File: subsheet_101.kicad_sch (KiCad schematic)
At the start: 0 parts

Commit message: place les principaux circuits -- il manque le symbole pour le PIA MC6821
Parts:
- added U?: GATE_ARRAY_MO5_V1_PHY, Package_LCC:PLCC-68_THT-Socket, symbol gate_array_v1:GATE_ARRAY_MO5_V1_PHY
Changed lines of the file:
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@@
 (kicad_sch (version 20211123) (generator eeschema)
-  (paper "A4")
+  (paper "A4" portrait)
   (title_block
     (date "2023-05-12")
     (rev "DRAFT")
   )
+  (symbol (lib_id "gate_array_v1:GATE_ARRAY_MO5_V1_PHY") (at 100.33 109.22 0) (unit 1)
+    (in_bom yes) (on_board yes)
+    (property "Reference" "U?" (id 0) (at 119.38 68.58 0)
+      (effects (font (size 1.27 1.27)) (justify left top))
+    )
+    (property "Value" "GATE_ARRAY_MO5_V1_PHY" (id 1) (at 119.38 71.12 0)
+      (effects (font (size 1.27 1.27) bold) (justify left top))
+    )
+    (property "Footprint" "Package_LCC:PLCC-68_THT-Socket" (id 2) (at 119.38 66.04 0)
+      (effects (font (size 1.27 1.27)) (justify left top) hide)
+    )
+    (property "Datasheet" "" (id 3) (at 100.33 109.22 0)
+      (effects (font (size 1.27 1.27)) hide)
+    )
+    (pin "1")
+    (pin "10")
+    (pin "11")
+    (pin "12")
+    (pin "13")
+    (pin "14")
+    (pin "15")
+    (pin "16")
+    (pin "17")
+    (pin "18")
+    (pin "19")
+    (pin "2")
+    (pin "20")
+    (pin "21")
+    (pin "22")
+    (pin "23")
+    (pin "24")
+    (pin "25")
+    (pin "26")
+    (pin "27")
+    (pin "28")
+    (pin "29")
+    (pin "3")
+    (pin "30")
+    (pin "31")
+    (pin "32")
+    (pin "33")
+    (pin "34")
+    (pin "35")
+    (pin "36")
+    (pin "37")
+    (pin "38")
+    (pin "39")
+    (pin "4")
+    (pin "40")
+    (pin "41")
+    (pin "42")
+    (pin "43")
+    (pin "44")
+    (pin "45")
+    (pin "46")
+    (pin "47")
+    (pin "48")
+    (pin "49")
+    (pin "5")
+    (pin "50")
+    (pin "51")
+    (pin "52")
+    (pin "53")
+    (pin "54")
+    (pin "55")
+    (pin "56")
+    (pin "57")
+    (pin "58")
+    (pin "59")
+    (pin "6")
+    (pin "60")
+    (pin "61")
+    (pin "62")
+    (pin "63")
+    (pin "64")
+    (pin "65")
+    (pin "66")
+    (pin "67")
+    (pin "68")
+    (pin "7")
+    (pin "8")
+    (pin "9")
+  )
 )

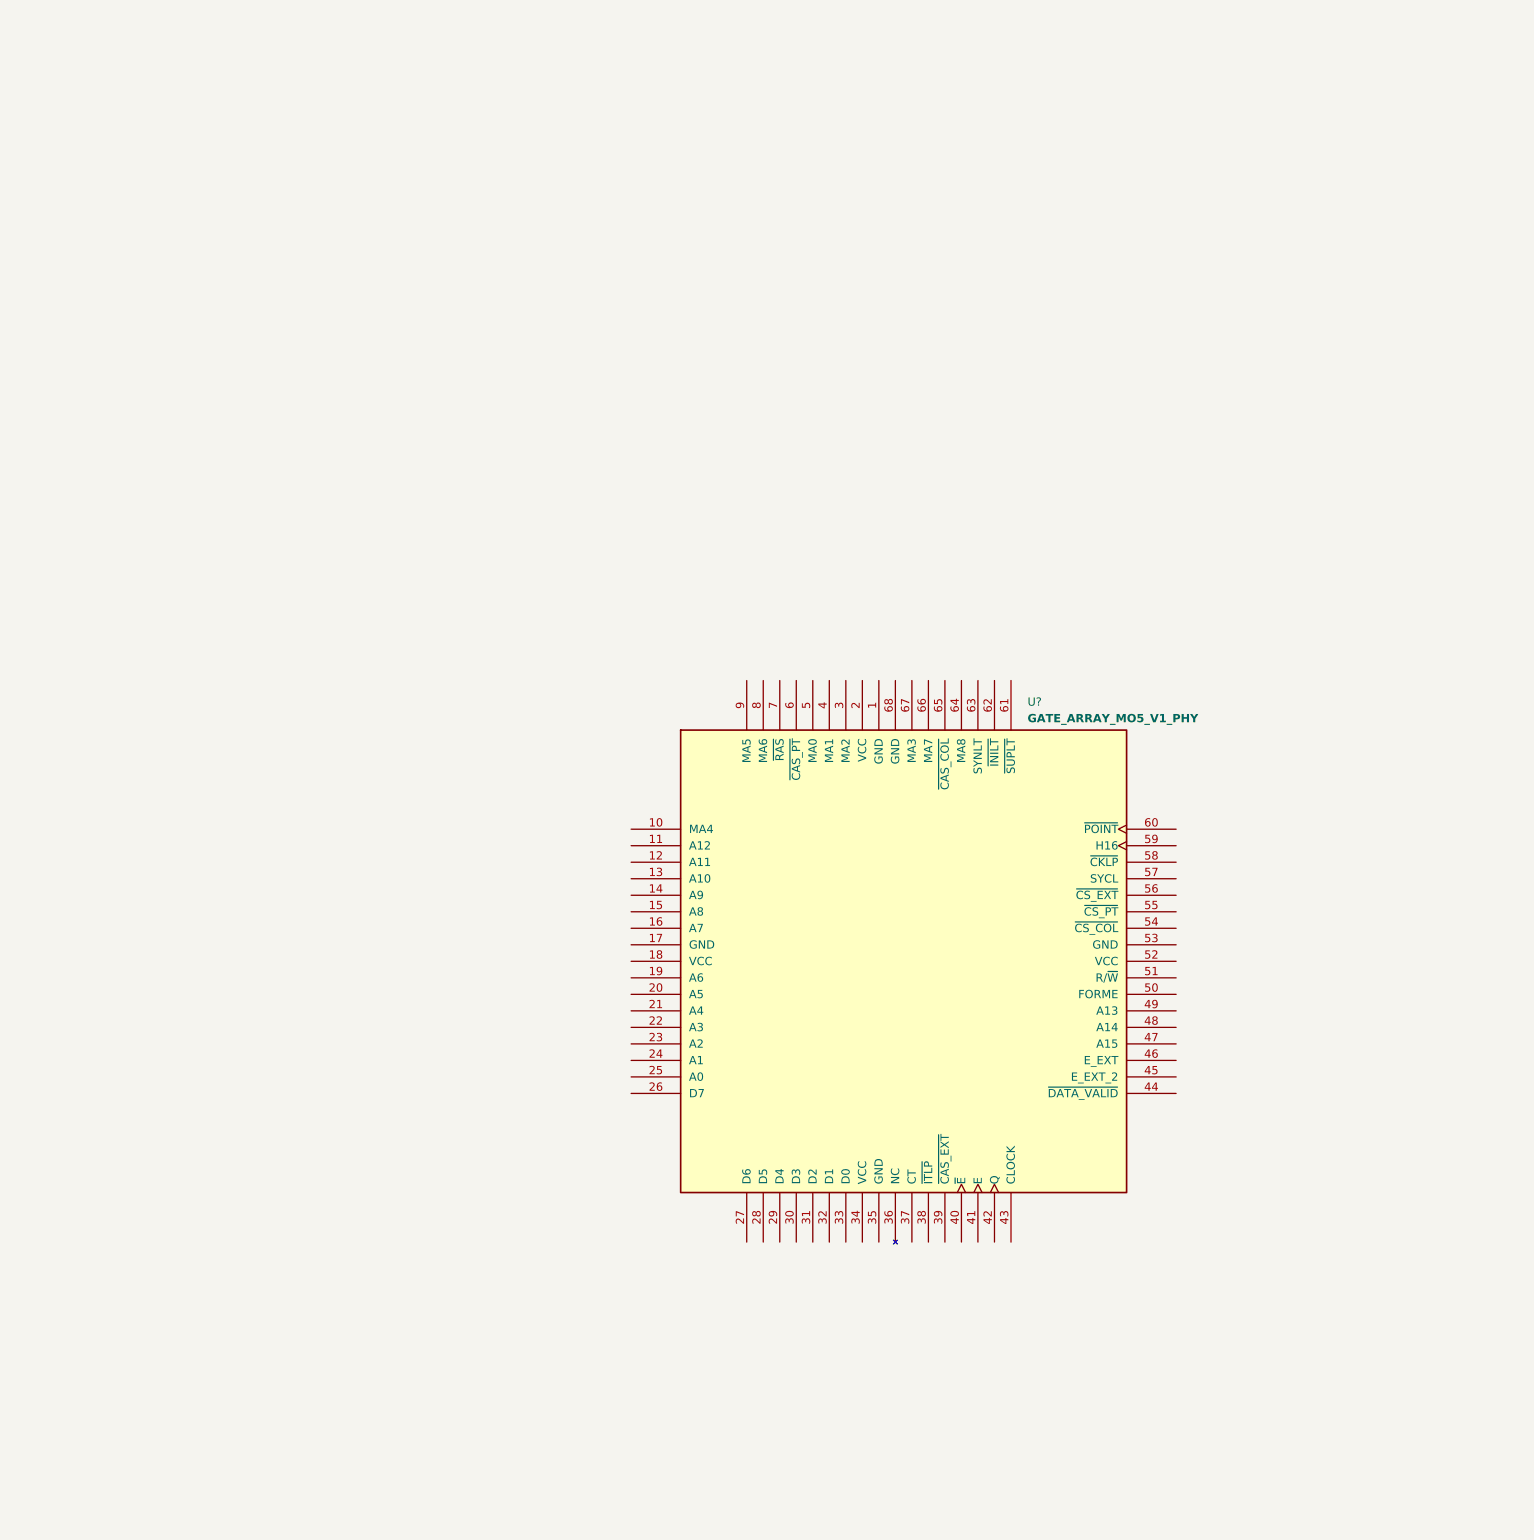
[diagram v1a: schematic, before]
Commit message: information schéma, commence le gate array I29
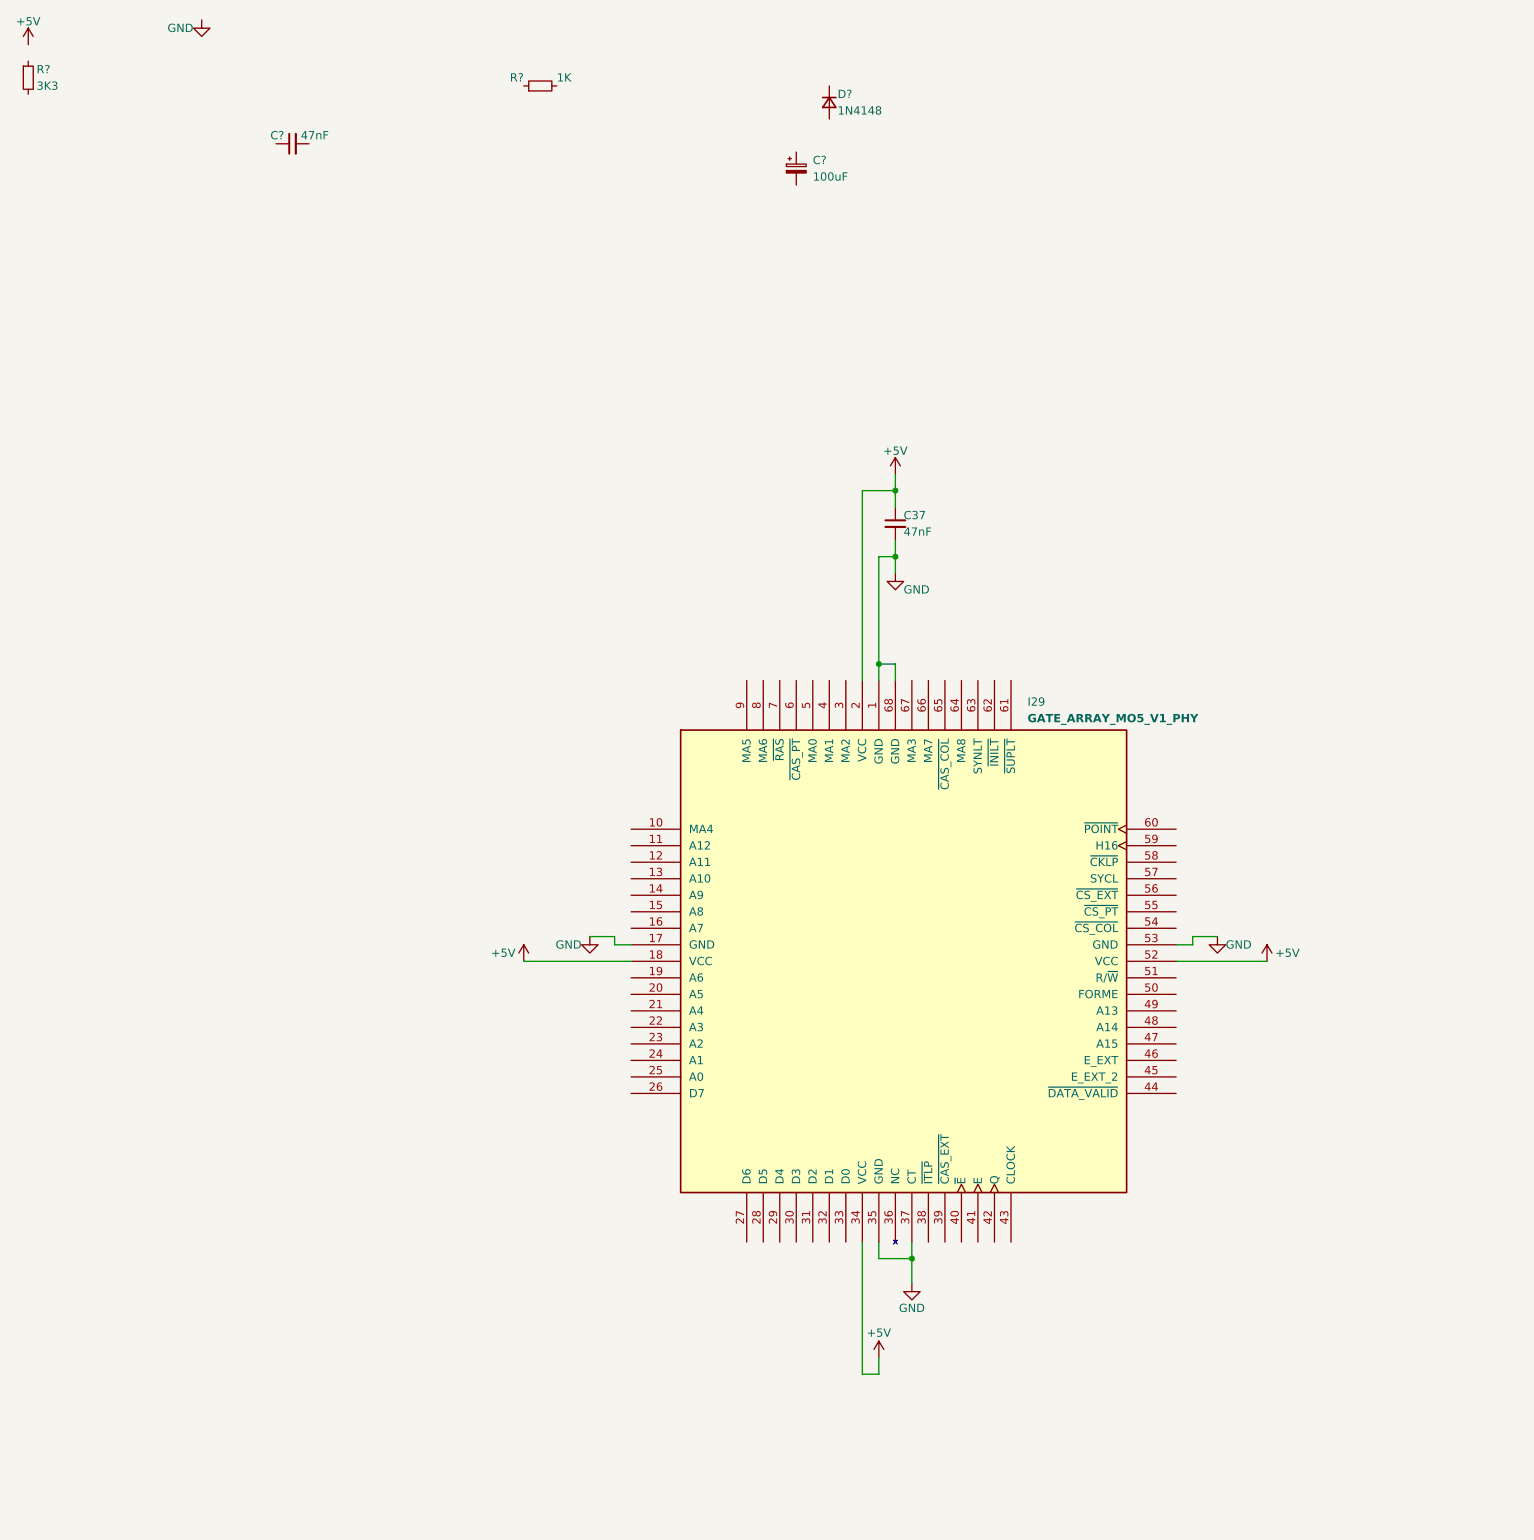
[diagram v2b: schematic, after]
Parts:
- added C37, C?: 47nF, symbol Device:C_Small
- added C?: 100uF, symbol Device:C_Polarized_Small
- added D?: 1N4148, symbol Device:D_Small
- added R?: 3K3, symbol Device:R_Small
- added R?: 1K, symbol Device:R_Small
- gave numbers to parts that had none: 1
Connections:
- net GND: now reaches I29.1 (GND)
- net GND: now also I29.17 (GND), I29.35 (GND), I29.37 (CT), I29.53 (GND), I29.68 (GND), C37.2
- net +5V: now reaches I29.18 (VCC)
- net +5V: now also I29.2 (VCC), I29.34 (VCC), I29.52 (VCC), C37.1
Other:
- title: (none) -> Conversion du Thomson MO5 — Unité centrale

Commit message: done I29, fixed address/databus mapping
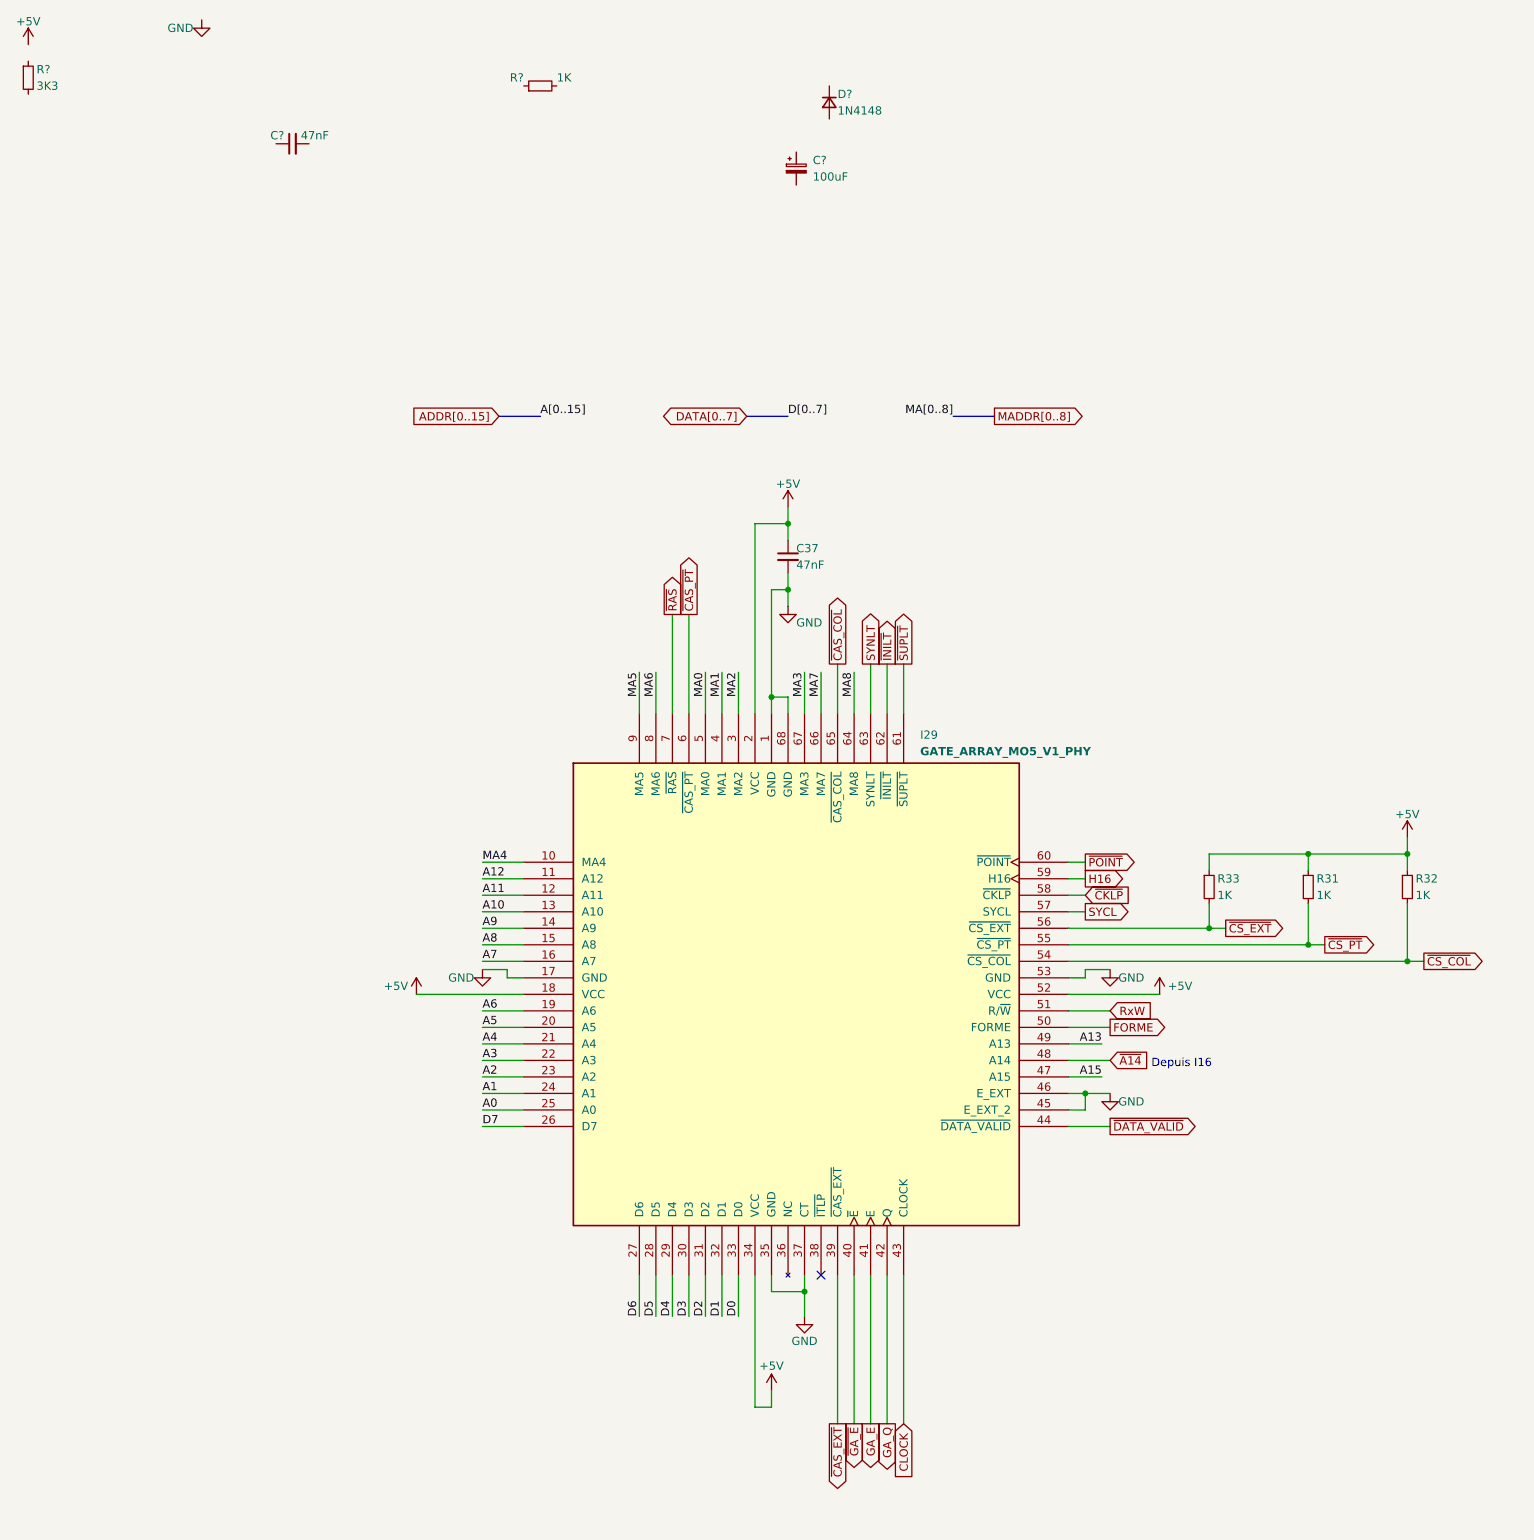
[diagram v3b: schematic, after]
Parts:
- added R31, R32, R33: 1K, symbol Device:R_Small
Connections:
- net +5V: now also R31.1, R32.1, R33.1
- net GND: now also I29.45 (E_EXT_2), I29.46 (E_EXT)
- net MA4: now reaches I29.10 (MA4)
- net A12: now reaches I29.11 (A12)
- net A11: now reaches I29.12 (A11)
- net A10: now reaches I29.13 (A10)
- net A9: now reaches I29.14 (A9)
- net A8: now reaches I29.15 (A8)
- net A7: now reaches I29.16 (A7)
- net A6: now reaches I29.19 (A6)
- net A5: now reaches I29.20 (A5)
- net A4: now reaches I29.21 (A4)
- net A3: now reaches I29.22 (A3)
- net A2: now reaches I29.23 (A2)
- net A1: now reaches I29.24 (A1)
- net A0: now reaches I29.25 (A0)
- net D7: now reaches I29.26 (D7)
- net D6: now reaches I29.27 (D6)
- net D5: now reaches I29.28 (D5)
- net D4: now reaches I29.29 (D4)
- net MA2: now reaches I29.3 (MA2)
- net D3: now reaches I29.30 (D3)
- net D2: now reaches I29.31 (D2)
- net D1: now reaches I29.32 (D1)
- net D0: now reaches I29.33 (D0)
- net ~{CAS_EXT}: now reaches I29.39 (~{CAS_EXT})
- net MA1: now reaches I29.4 (MA1)
- net ~{GA_E}: now reaches I29.40 (~{E})
- net GA_E: now reaches I29.41 (E)
- net GA_Q: now reaches I29.42 (Q)
- net CLOCK: now reaches I29.43 (CLOCK)
- net ~{DATA_VALID}: now reaches I29.44 (~{DATA_VALID})
- net A15: now reaches I29.47 (A15)
- net ~{A14}: now reaches I29.48 (A14)
- net A13: now reaches I29.49 (A13)
- net MA0: now reaches I29.5 (MA0)
- net FORME: now reaches I29.50 (FORME)
- net RxW: now reaches I29.51 (R/~{W})
- net ~{CS_COL}: now reaches I29.54 (~{CS_COL})
- net ~{CS_COL}: now also R32.2
- net ~{CS_PT}: now reaches I29.55 (~{CS_PT})
- net ~{CS_PT}: now also R31.2
- net ~{CS_EXT}: now reaches I29.56 (~{CS_EXT})
- net ~{CS_EXT}: now also R33.2
- net SYCL: now reaches I29.57 (SYCL)
- net ~{CKLP}: now reaches I29.58 (~{CKLP})
- net H16: now reaches I29.59 (H16)
- net ~{CAS_PT}: now reaches I29.6 (~{CAS_PT})
- net ~{POINT}: now reaches I29.60 (~{POINT})
- net ~{SUPLT}: now reaches I29.61 (~{SUPLT})
- net ~{INILT}: now reaches I29.62 (~{INILT})
- net SYNLT: now reaches I29.63 (SYNLT)
- net MA8: now reaches I29.64 (MA8)
- net ~{CAS_COL}: now reaches I29.65 (~{CAS_COL})
- net MA7: now reaches I29.66 (MA7)
- net MA3: now reaches I29.67 (MA3)
- net ~{RAS}: now reaches I29.7 (~{RAS})
- net MA6: now reaches I29.8 (MA6)
- net MA5: now reaches I29.9 (MA5)
- no-connect marks 0 -> 1
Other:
- note added: "Depuis I16"
- moved on the sheet: C37, I29
